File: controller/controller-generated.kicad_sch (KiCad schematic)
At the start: 12 parts, among them J1 USB-C, J2 Thermocouple, J3 IEC C14, J4 AC Outlet, SW1 Rotary Encoder, U1 ESP32-DevKitC, U2 MAX31856

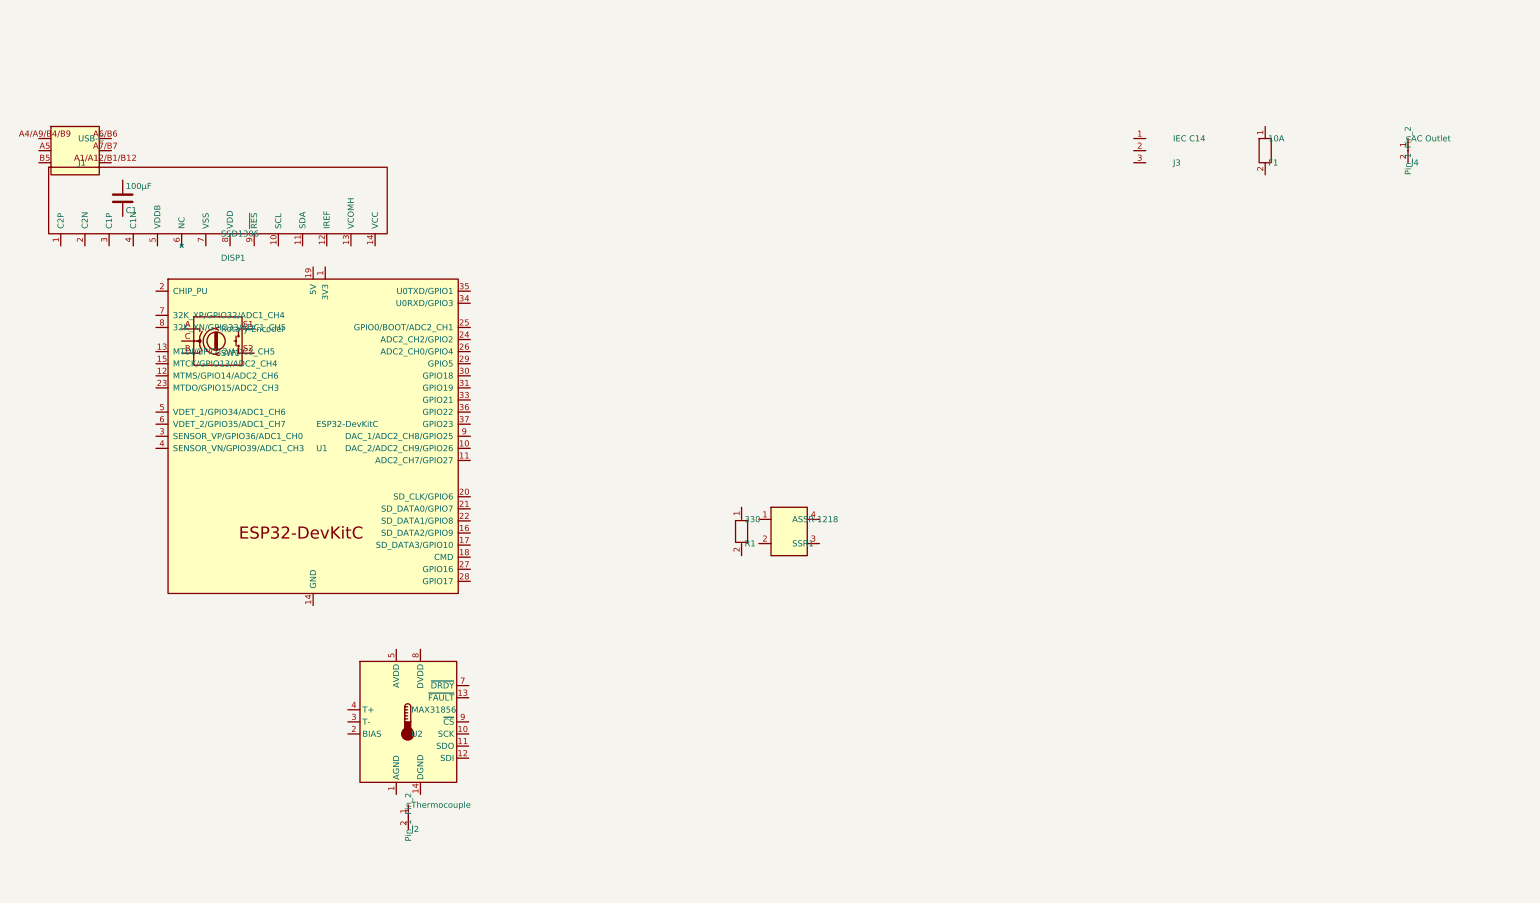
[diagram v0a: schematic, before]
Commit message: fix: add power flags to generated schematic
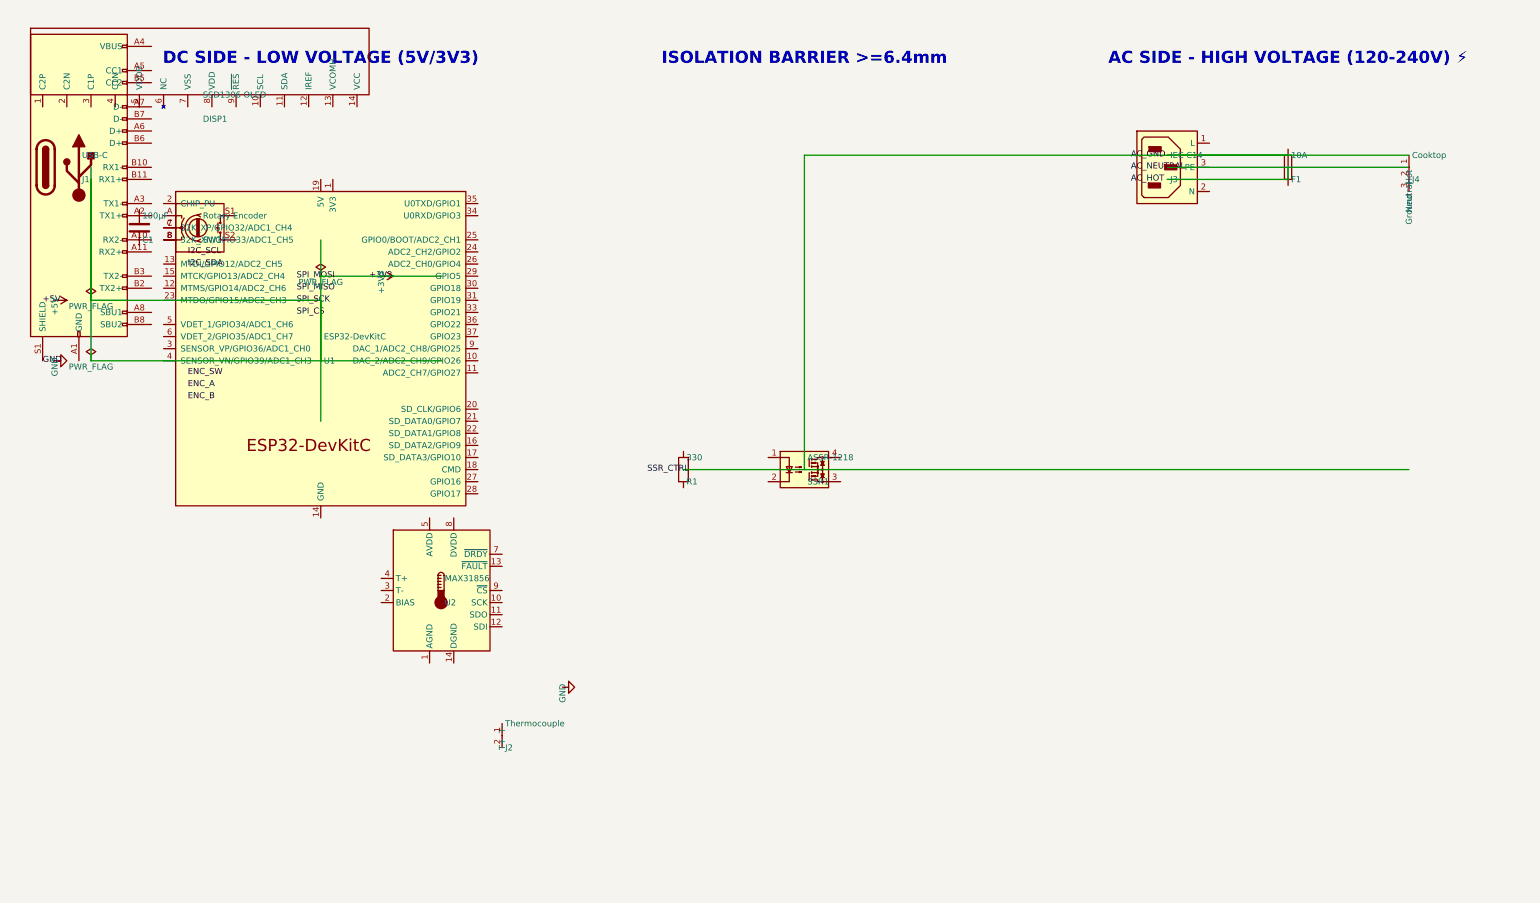
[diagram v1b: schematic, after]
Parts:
- removed C1: 100µF, symbol C
- removed DISP1: SSD1306, symbol SSD1306
- removed F1: 10A, symbol Fuse
- removed J1: USB-C, symbol USB_C_Receptacle
- removed J2: Thermocouple, symbol Conn_01x02
- removed J3: IEC C14, symbol IEC_60320_C14_Receptacle
- removed J4: AC Outlet, symbol Conn_01x02
- removed R1: 330, symbol R
- removed SSR1: ASSR-1218, symbol ASSR-1218
- removed SW1: Rotary Encoder, symbol RotaryEncoder_Switch
- removed U1: ESP32-DevKitC, symbol ESP32-DevKitC
- removed U2: MAX31856, symbol MAX31856
- added C1: 100µF, Capacitor_THT:CP_Radial_D8.0mm_P3.50mm, symbol Device:C
- added DISP1: SSD1306 OLED, SSD1306_OLED:SSD1306_OLED-0.91-128x32, symbol SSD1306_OLED:SSD1306
- added F1: 10A, Fuse:Fuseholder_Cylinder-5x20mm_Schurter_0031_8003_Straight, symbol Device:Fuse
- added J1: USB-C, Connector_USB:USB_C_Receptacle_GCT_USB4085, symbol Connector:USB_C_Receptacle
- added J2: Thermocouple, Connector_Wire:Screw_Terminal_01x02, symbol Custom:Thermocouple_Connector
- added J3: IEC C14, Connector_AC:IEC_60320_C14_PanelMount, symbol Connector:IEC_60320_C14_Receptacle
- added J4: Cooktop, TerminalBlock:TerminalBlock_bornier-3_P5.08mm, symbol Custom:AC_Outlet_Connector
- added R1: 330, Resistor_SMD:R_1206_3216Metric, symbol Device:R
- added SSR1: ASSR-1218, Package_SO:SOIC-8_3.9x4.9mm_P1.27mm, symbol Relay_SolidState:ASSR-1218
- added SW1: Rotary Encoder, Rotary_Encoder:RotaryEncoder_Alps_EC11E-Switch_Vertical, symbol Device:RotaryEncoder_Switch
- added U1: ESP32-DevKitC, Espressif:ESP32-DevKitC, symbol Espressif:ESP32-DevKitC
- added U2: MAX31856, Package_SO:SOIC-20W_7.5x12.8mm_P1.27mm, symbol Sensor_Temperature:MAX31856
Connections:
- new net: J1.A1 (GND), J1.A12 (GND), J1.B1 (GND), J1.B12 (GND)
- new net: J1.A4 (VBUS), J1.A9 (VBUS), J1.B4 (VBUS), J1.B9 (VBUS)
- new net: U1.14 (GND), U1.32 (GND), U1.38 (GND)
- new net: SW1.C, U1.7 (32K_XP/GPIO32/ADC1_CH4)
- new net: SW1.B, U1.8 (32K_XN/GPIO33/ADC1_CH5)
- new net AC_GND: J4.1 (Hot)
- new net GND: J1.S1 (SHIELD)
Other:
- note added: "AC SIDE - HIGH VOLTAGE (120-240V) ⚡"
- note added: "DC SIDE - LOW VOLTAGE (5V/3V3)"
- note added: "ISOLATION BARRIER >=6.4mm"
- company: Project Author -> (none)

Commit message: feat: wire up ssr and ac nets
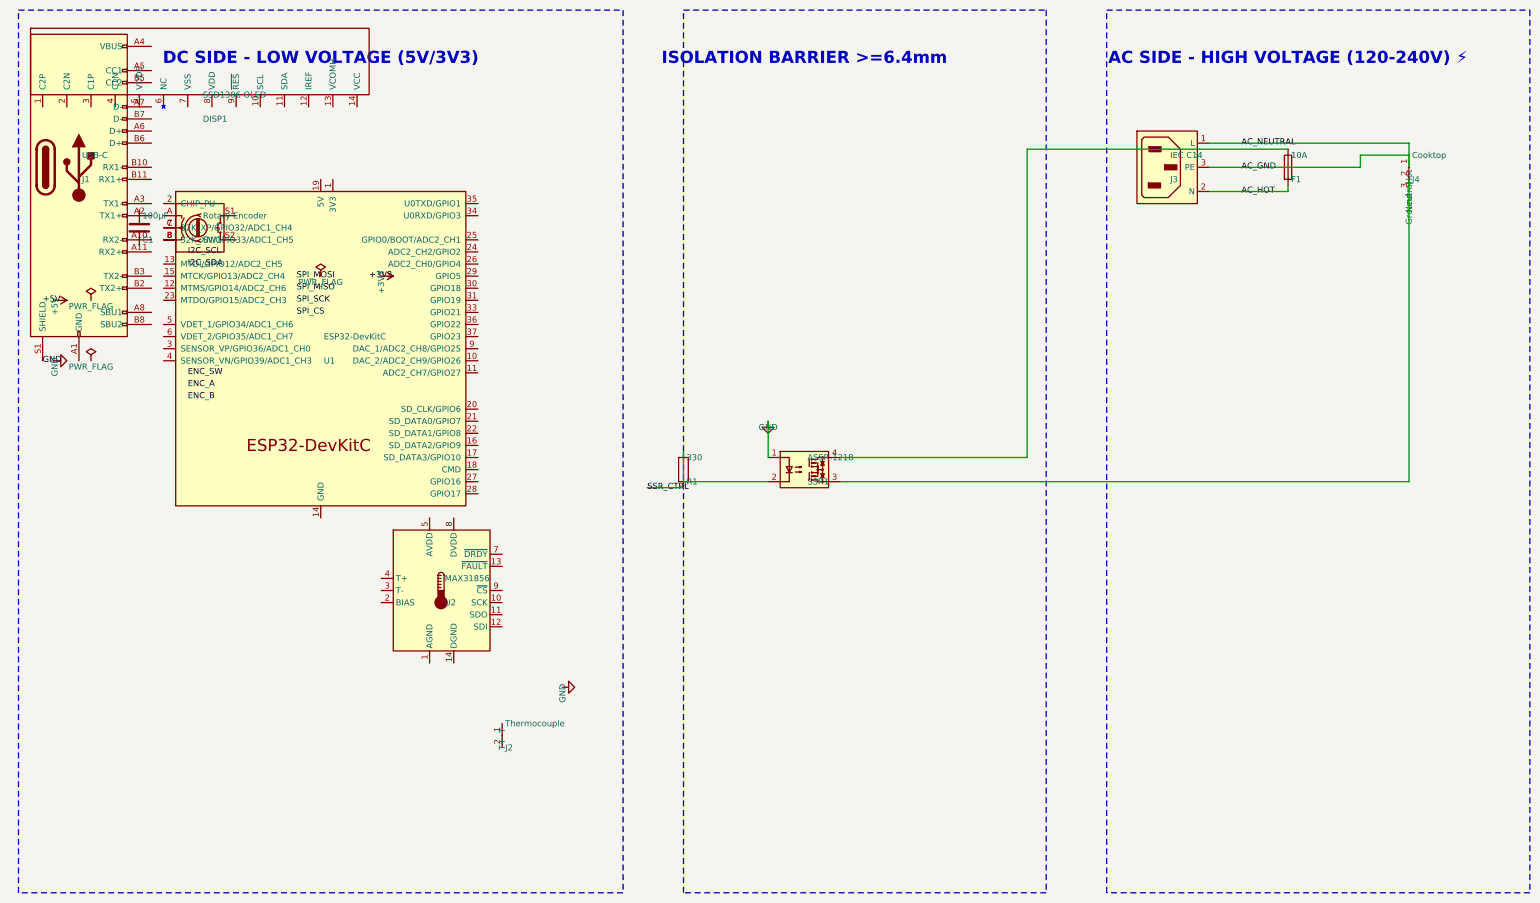
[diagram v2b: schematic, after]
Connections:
- net AC_GND: now also J3.3 (PE)
- net AC_HOT: now also F1.2, J3.2 (N)
- net AC_NEUTRAL: now also J3.1 (L), J4.2 (Neutral)
- net GND: now also SSR1.1
- net SSR_CTRL: now also R1.2
- net at F1.1: now also SSR1.4
- net at J4.3 (Ground): now also SSR1.3
- net at R1.1: now also SSR1.2
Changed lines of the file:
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@@
   (effects (font (size 2.54 2.54) (bold yes)))
 )
+(polyline
+  (pts (xy 38.1 30.48) (xy 165.1 30.48) (xy 165.1 215.9) (xy 38.1 215.9) (xy 38.1 30.48))
+  (stroke (width 0.254) (type dash))
+)
+(polyline
+  (pts (xy 177.8 30.48) (xy 254.0 30.48) (xy 254.0 215.9) (xy 177.8 215.9) (xy 177.8 30.48))
+  (stroke (width 0.254) (type dash))
+)
+(polyline
+  (pts (xy 266.7 30.48) (xy 355.6 30.48) (xy 355.6 215.9) (xy 266.7 215.9) (xy 266.7 30.48))
+  (stroke (width 0.254) (type dash))
+)
           (symbol (lib_id "Connector:USB_C_Receptacle") (at 50.8 63.5 0) (unit 1)
   (exclude_from_sim no) (in_bom yes) (on_board yes) (dnp no)
@@
   )
 )
+(symbol (lib_id "power:GND") (at 195.58 116.84 0) (unit 1)
+  (exclude_from_sim no) (in_bom no) (on_board no) (dnp no)
+  (property "Reference" "#PWR0105" (at 195.58 113.03 0)
+    (effects (font (size 1.27 1.27)) (hide yes))
+  )
+  (property "Value" "GND" (at 195.58 118.11 0)
+    (effects (font (size 1.27 1.27)))
+  )
+  (property "Footprint" "" (at 195.58 116.84 0)
+    (effects (font (size 1.27 1.27)) (hide yes))
+  )
+  (property "Datasheet" "" (at 195.58 116.84 0)
+    (effects (font (size 1.27 1.27)) (hide yes))
+  )
+)
 (symbol (lib_id "power:PWR_FLAG") (at 53.34 91.44 0) (unit 1)
   (exclude_from_sim no) (in_bom no) (on_board no) (dnp no)
@@
           (wire
   (pts
-    (xy 53.34 63.5) (xy 53.34 76.2)
-  )
-  (stroke
-    (width 0.2032)
-    (type default)
-  )
-)
-(wire
-  (pts
-    (xy 53.34 76.2) (xy 53.34 91.44)
-  )
-  (stroke
-    (width 0.2032)
-    (type default)
-  )
-)
-(wire
-  (pts
-    (xy 53.34 91.44) (xy 101.6 91.44)
-  )
-  (stroke
-    (width 0.2032)
-    (type default)
-  )
-)
-(wire
-  (pts
-    (xy 53.34 66.04) (xy 53.34 104.14)
-  )
-  (stroke
-    (width 0.2032)
-    (type default)
-  )
-)
-(wire
-  (pts
-    (xy 53.34 104.14) (xy 101.6 104.14)
-  )
-  (stroke
-    (width 0.2032)
-    (type default)
-  )
-)
-(wire
-  (pts
-    (xy 101.6 104.14) (xy 127.0 104.14)
-  )
-  (stroke
-    (width 0.2032)
-    (type default)
-  )
-)
-(wire
-  (pts
-    (xy 101.6 86.36) (xy 127.0 86.36)
-  )
-  (stroke
-    (width 0.2032)
-    (type default)
-  )
-)
-(wire
-  (pts
-    (xy 101.6 91.44) (xy 101.6 116.84)
-  )
-  (stroke
-    (width 0.2032)
-    (type default)
-  )
-)
-(wire
-  (pts
-    (xy 101.6 104.14) (xy 101.6 78.74)
-  )
-  (stroke
-    (width 0.2032)
-    (type default)
-  )
-)
-(wire
-  (pts
-    (xy 177.8 127.0) (xy 203.2 127.0)
-  )
-  (stroke
-    (width 0.2032)
-    (type default)
-  )
-)
-(wire
-  (pts
-    (xy 203.2 127.0) (xy 330.2 127.0)
-  )
-  (stroke
-    (width 0.2032)
-    (type default)
-  )
-)
-(wire
-  (pts
-    (xy 279.4 66.04) (xy 304.8 66.04)
-  )
-  (stroke
-    (width 0.2032)
-    (type default)
-  )
-)
-(wire
-  (pts
-    (xy 304.8 66.04) (xy 304.8 63.5)
-  )
-  (stroke
-    (width 0.2032)
-    (type default)
-  )
-)
-(wire
-  (pts
-    (xy 304.8 60.96) (xy 203.2 60.96)
-  )
-  (stroke
-    (width 0.2032)
-    (type default)
-  )
-)
-(wire
-  (pts
-    (xy 203.2 60.96) (xy 203.2 127.0)
-  )
-  (stroke
-    (width 0.2032)
-    (type default)
-  )
-)
-(wire
-  (pts
-    (xy 279.4 63.5) (xy 330.2 63.5)
-  )
-  (stroke
-    (width 0.2032)
-    (type default)
-  )
-)
-(wire
-  (pts
-    (xy 279.4 60.96) (xy 330.2 60.96)
+    (xy 170.18 130.81) (xy 177.8 130.81)
+  )
+  (stroke
+    (width 0.2032)
+    (type default)
+  )
+)
+(wire
+  (pts
+    (xy 177.8 123.19) (xy 177.8 129.54)
+  )
+  (stroke
+    (width 0.2032)
+    (type default)
+  )
+)
+(wire
+  (pts
+    (xy 177.8 129.54) (xy 195.58 129.54)
+  )
+  (stroke
+    (width 0.2032)
+    (type default)
+  )
+)
+(wire
+  (pts
+    (xy 195.58 124.46) (xy 195.58 118.11)
+  )
+  (stroke
+    (width 0.2032)
+    (type default)
+  )
+)
+(wire
+  (pts
+    (xy 195.58 118.11) (xy 195.58 116.84)
+  )
+  (stroke
+    (width 0.2032)
+    (type default)
+  )
+)
+(wire
+  (pts
+    (xy 288.29 68.58) (xy 304.8 68.58)
+  )
+  (stroke
+    (width 0.2032)
+    (type default)
+  )
+)
+(wire
+  (pts
+    (xy 304.8 68.58) (xy 304.8 67.31)
+  )
+  (stroke
+    (width 0.2032)
+    (type default)
+  )
+)
+(wire
+  (pts
+    (xy 304.8 59.69) (xy 250.0 59.69)
+  )
+  (stroke
+    (width 0.2032)
+    (type default)
+  )
+)
+(wire
+  (pts
+    (xy 250.0 59.69) (xy 250.0 124.46)
+  )
+  (stroke
+    (width 0.2032)
+    (type default)
+  )
+)
+(wire
+  (pts
+    (xy 250.0 124.46) (xy 210.82 124.46)
+  )
+  (stroke
+    (width 0.2032)
+    (type default)
+  )
+)
+(wire
+  (pts
+    (xy 210.82 129.54) (xy 330.2 129.54)
+  )
+  (stroke
+    (width 0.2032)
+    (type default)
+  )
+)
+(wire
+  (pts
+    (xy 330.2 129.54) (xy 330.2 66.04)
+  )
+  (stroke
+    (width 0.2032)
+    (type default)
+  )
+)
+(wire
+  (pts
+    (xy 288.29 58.42) (xy 330.2 58.42)
+  )
+  (stroke
+    (width 0.2032)
+    (type default)
+  )
+)
+(wire
+  (pts
+    (xy 330.2 58.42) (xy 330.2 63.5)
+  )
+  (stroke
+    (width 0.2032)
+    (type default)
+  )
+)
+(wire
+  (pts
+    (xy 288.29 63.5) (xy 320.0 63.5)
+  )
+  (stroke
+    (width 0.2032)
+    (type default)
+  )
+)
+(wire
+  (pts
+    (xy 320.0 63.5) (xy 320.0 60.96)
+  )
+  (stroke
+    (width 0.2032)
+    (type default)
+  )
+)
+(wire
+  (pts
+    (xy 320.0 60.96) (xy 330.2 60.96)
   )
   (stroke
@@
   (effects (font (size 1.27 1.27)) (justify left))
 )
-(label "SSR_CTRL" (at 170.18 127.0 0)
-  (effects (font (size 1.27 1.27)) (justify left))
-)
-(label "AC_HOT" (at 271.78 66.04 0)
-  (effects (font (size 1.27 1.27)) (justify left))
-)
-(label "AC_NEUTRAL" (at 271.78 63.5 0)
-  (effects (font (size 1.27 1.27)) (justify left))
-)
-(label "AC_GND" (at 271.78 60.96 0)
-  (effects (font (size 1.27 1.27)) (justify left))
-)
+(label "SSR_CTRL" (at 170.18 130.81 0)
+  (effects (font (size 1.27 1.27)) (justify left))
+)
+(label "AC_HOT" (at 295.0 68.58 0)
+  (effects (font (size 1.27 1.27)) (justify left))
+)
+(label "AC_NEUTRAL" (at 295.0 58.42 0)
+  (effects (font (size 1.27 1.27)) (justify left))
+)
+(label "AC_GND" (at 295.0 63.5 0)
+  (effects (font (size 1.27 1.27)) (justify left))
+)

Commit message: fix: stabilize ac net connections
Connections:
- net AC_HOT: now also J3.1 (L); no longer J3.2 (N)
- net AC_NEUTRAL: now also J3.2 (N); no longer J3.1 (L)
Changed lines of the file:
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@@
 (wire
   (pts
-    (xy 288.29 68.58) (xy 304.8 68.58)
+    (xy 288.29 58.42) (xy 304.8 58.42)
+  )
+  (stroke
+    (width 0.2032)
+    (type default)
+  )
+)
+(wire
+  (pts
+    (xy 304.8 58.42) (xy 304.8 68.58)
   )
   (stroke
@@
 (wire
   (pts
-    (xy 304.8 59.69) (xy 250.0 59.69)
+    (xy 304.8 59.69) (xy 248.92 59.69)
   )
   (stroke
@@
 (wire
   (pts
-    (xy 250.0 59.69) (xy 250.0 124.46)
+    (xy 248.92 59.69) (xy 248.92 124.46)
   )
   (stroke
@@
 (wire
   (pts
-    (xy 250.0 124.46) (xy 210.82 124.46)
+    (xy 248.92 124.46) (xy 210.82 124.46)
   )
   (stroke
@@
 (wire
   (pts
-    (xy 210.82 129.54) (xy 330.2 129.54)
+    (xy 210.82 129.54) (xy 320.04 129.54)
   )
   (stroke
@@
 (wire
   (pts
-    (xy 330.2 129.54) (xy 330.2 66.04)
+    (xy 320.04 129.54) (xy 320.04 66.04)
   )
   (stroke
@@
 (wire
   (pts
-    (xy 288.29 58.42) (xy 330.2 58.42)
+    (xy 320.04 66.04) (xy 330.2 66.04)
   )
   (stroke
@@
 (wire
   (pts
-    (xy 330.2 58.42) (xy 330.2 63.5)
+    (xy 288.29 68.58) (xy 330.2 68.58)
   )
   (stroke
@@
 (wire
   (pts
-    (xy 288.29 63.5) (xy 320.0 63.5)
+    (xy 330.2 68.58) (xy 330.2 63.5)
   )
   (stroke
@@
 (wire
   (pts
-    (xy 320.0 63.5) (xy 320.0 60.96)
+    (xy 288.29 63.5) (xy 320.04 63.5)
   )
   (stroke
@@
 (wire
   (pts
-    (xy 320.0 60.96) (xy 330.2 60.96)
+    (xy 320.04 63.5) (xy 320.04 60.96)
+  )
+  (stroke
+    (width 0.2032)
+    (type default)
+  )
+)
+(wire
+  (pts
+    (xy 320.04 60.96) (xy 330.2 60.96)
   )
   (stroke
@@
   (effects (font (size 1.27 1.27)) (justify left))
 )
-(label "AC_HOT" (at 295.0 68.58 0)
+(label "AC_HOT" (at 295.0 58.42 0)
   (effects (font (size 1.27 1.27)) (justify left))
 )
-(label "AC_NEUTRAL" (at 295.0 58.42 0)
+(label "AC_NEUTRAL" (at 295.0 68.58 0)
   (effects (font (size 1.27 1.27)) (justify left))
 )
